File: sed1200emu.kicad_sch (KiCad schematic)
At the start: 17 parts, among them CN1 PINHD-1X6, CN2 PINHD-1X6, IC1 MEGA8-AI, Q1 CRYSTALHC49S

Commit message: Replace MEGA8 Symbol and Footprint
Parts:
- IC1: footprint sed1200emu:TQFP32-08 -> Package_QFP:TQFP-32_7x7mm_P0.8mm
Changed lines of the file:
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@@
   (symbol (lib_id "sed1200emu-eagle-import:VCC") (at 180.34 93.98 90) (unit 1)
     (in_bom yes) (on_board yes) (dnp no)
-    (property "Reference" "#P+3" (at 180.34 93.98 0)
+    (property "Reference" "#P+03" (at 180.34 93.98 0)
       (effects (font (size 1.27 1.27)) hide)
     )
@@
       (project "sed1200emu"
         (path "/123507c6-0003-4611-af8b-4b1000037212"
-          (reference "#P+3") (unit 1)
+          (reference "#P+03") (unit 1)
         )
       )
@@
   (symbol (lib_id "sed1200emu-eagle-import:GND") (at 185.42 66.04 270) (unit 1)
     (in_bom yes) (on_board yes) (dnp no)
-    (property "Reference" "#GND2" (at 185.42 66.04 0)
+    (property "Reference" "#GND02" (at 185.42 66.04 0)
       (effects (font (size 1.27 1.27)) hide)
     )
@@
       (project "sed1200emu"
         (path "/123507c6-0003-4611-af8b-4b1000037212"
-          (reference "#GND2") (unit 1)
+          (reference "#GND02") (unit 1)
         )
       )
@@
   (symbol (lib_id "sed1200emu-eagle-import:GND") (at 198.12 91.44 270) (unit 1)
     (in_bom yes) (on_board yes) (dnp no)
-    (property "Reference" "#GND3" (at 198.12 91.44 0)
+    (property "Reference" "#GND03" (at 198.12 91.44 0)
       (effects (font (size 1.27 1.27)) hide)
     )
@@
       (project "sed1200emu"
         (path "/123507c6-0003-4611-af8b-4b1000037212"
-          (reference "#GND3") (unit 1)
+          (reference "#GND03") (unit 1)
         )
       )
@@
   (symbol (lib_id "sed1200emu-eagle-import:VCC") (at 165.1 127 90) (unit 1)
     (in_bom yes) (on_board yes) (dnp no)
-    (property "Reference" "#P+4" (at 165.1 127 0)
+    (property "Reference" "#P+04" (at 165.1 127 0)
       (effects (font (size 1.27 1.27)) hide)
     )
@@
       (project "sed1200emu"
         (path "/123507c6-0003-4611-af8b-4b1000037212"
-          (reference "#P+4") (unit 1)
+          (reference "#P+04") (unit 1)
         )
       )
@@
   (symbol (lib_id "sed1200emu-eagle-import:GND") (at 68.58 78.74 270) (unit 1)
     (in_bom yes) (on_board yes) (dnp no)
-    (property "Reference" "#GND9" (at 68.58 78.74 0)
+    (property "Reference" "#GND09" (at 68.58 78.74 0)
       (effects (font (size 1.27 1.27)) hide)
     )
@@
       (project "sed1200emu"
         (path "/123507c6-0003-4611-af8b-4b1000037212"
-          (reference "#GND9") (unit 1)
+          (reference "#GND09") (unit 1)
         )
       )
@@
   (symbol (lib_id "sed1200emu-eagle-import:GND") (at 198.12 129.54 270) (unit 1)
     (in_bom yes) (on_board yes) (dnp no)
-    (property "Reference" "#GND10" (at 198.12 129.54 0)
+    (property "Reference" "#GND010" (at 198.12 129.54 0)
       (effects (font (size 1.27 1.27)) hide)
     )
@@
       (project "sed1200emu"
         (path "/123507c6-0003-4611-af8b-4b1000037212"
-          (reference "#GND10") (unit 1)
+          (reference "#GND010") (unit 1)
         )
       )
@@
       (effects (font (size 1.778 1.5113)) (justify left bottom))
     )
-    (property "Footprint" "sed1200emu:TQFP32-08" (at 124.46 86.36 0)
-      (effects (font (size 1.27 1.27)) hide)
-    )
-    (property "Datasheet" "" (at 124.46 86.36 0)
+    (property "Footprint" "Package_QFP:TQFP-32_7x7mm_P0.8mm" (at 124.46 86.36 0)
+      (effects (font (size 1.27 1.27)) hide)
+    )
+    (property "Datasheet" "http://ww1.microchip.com/downloads/en/DeviceDoc/atmel-2486-8-bit-avr-microcontroller-atmega8_l_datasheet.pdf" (at 124.46 86.36 0)
       (effects (font (size 1.27 1.27)) hide)
     )
@@
   (symbol (lib_id "sed1200emu-eagle-import:GND") (at 93.98 109.22 0) (unit 1)
     (in_bom yes) (on_board yes) (dnp no)
-    (property "Reference" "#GND4" (at 93.98 109.22 0)
+    (property "Reference" "#GND04" (at 93.98 109.22 0)
       (effects (font (size 1.27 1.27)) hide)
     )
@@
       (project "sed1200emu"
         (path "/123507c6-0003-4611-af8b-4b1000037212"
-          (reference "#GND4") (unit 1)
+          (reference "#GND04") (unit 1)
         )
       )
@@
   (symbol (lib_id "sed1200emu-eagle-import:VCC") (at 81.28 48.26 0) (unit 1)
     (in_bom yes) (on_board yes) (dnp no)
-    (property "Reference" "#P+6" (at 81.28 48.26 0)
+    (property "Reference" "#P+06" (at 81.28 48.26 0)
       (effects (font (size 1.27 1.27)) hide)
     )
@@
       (project "sed1200emu"
         (path "/123507c6-0003-4611-af8b-4b1000037212"
-          (reference "#P+6") (unit 1)
+          (reference "#P+06") (unit 1)
         )
       )
@@
   (symbol (lib_id "sed1200emu-eagle-import:VCC") (at 86.36 71.12 90) (unit 1)
     (in_bom yes) (on_board yes) (dnp no)
-    (property "Reference" "#P+2" (at 86.36 71.12 0)
+    (property "Reference" "#P+02" (at 86.36 71.12 0)
       (effects (font (size 1.27 1.27)) hide)
     )
@@
       (project "sed1200emu"
         (path "/123507c6-0003-4611-af8b-4b1000037212"
-          (reference "#P+2") (unit 1)
+          (reference "#P+02") (unit 1)
         )
       )
@@
   (symbol (lib_id "sed1200emu-eagle-import:VCC") (at 187.96 142.24 270) (unit 1)
     (in_bom yes) (on_board yes) (dnp no)
-    (property "Reference" "#P+5" (at 187.96 142.24 0)
+    (property "Reference" "#P+05" (at 187.96 142.24 0)
       (effects (font (size 1.27 1.27)) hide)
     )
@@
       (project "sed1200emu"
         (path "/123507c6-0003-4611-af8b-4b1000037212"
-          (reference "#P+5") (unit 1)
+          (reference "#P+05") (unit 1)
         )
       )
@@
   (symbol (lib_id "sed1200emu-eagle-import:GND") (at 99.06 109.22 0) (unit 1)
     (in_bom yes) (on_board yes) (dnp no)
-    (property "Reference" "#GND1" (at 99.06 109.22 0)
+    (property "Reference" "#GND01" (at 99.06 109.22 0)
       (effects (font (size 1.27 1.27)) hide)
     )
@@
       (project "sed1200emu"
         (path "/123507c6-0003-4611-af8b-4b1000037212"
-          (reference "#GND1") (unit 1)
+          (reference "#GND01") (unit 1)
         )
       )
@@
   (symbol (lib_id "sed1200emu-eagle-import:VCC") (at 182.88 45.72 90) (unit 1)
     (in_bom yes) (on_board yes) (dnp no)
-    (property "Reference" "#P+1" (at 182.88 45.72 0)
+    (property "Reference" "#P+01" (at 182.88 45.72 0)
       (effects (font (size 1.27 1.27)) hide)
     )
@@
       (project "sed1200emu"
         (path "/123507c6-0003-4611-af8b-4b1000037212"
-          (reference "#P+1") (unit 1)
+          (reference "#P+01") (unit 1)
         )
       )
@@
   (symbol (lib_id "sed1200emu-eagle-import:GND") (at 88.9 109.22 0) (unit 1)
     (in_bom yes) (on_board yes) (dnp no)
-    (property "Reference" "#GND5" (at 88.9 109.22 0)
+    (property "Reference" "#GND05" (at 88.9 109.22 0)
       (effects (font (size 1.27 1.27)) hide)
     )
@@
       (project "sed1200emu"
         (path "/123507c6-0003-4611-af8b-4b1000037212"
-          (reference "#GND5") (unit 1)
+          (reference "#GND05") (unit 1)
         )
       )
@@
   (symbol (lib_id "sed1200emu-eagle-import:GND") (at 182.88 160.02 0) (unit 1)
     (in_bom yes) (on_board yes) (dnp no)
-    (property "Reference" "#GND7" (at 182.88 160.02 0)
+    (property "Reference" "#GND07" (at 182.88 160.02 0)
       (effects (font (size 1.27 1.27)) hide)
     )
@@
       (project "sed1200emu"
         (path "/123507c6-0003-4611-af8b-4b1000037212"
-          (reference "#GND7") (unit 1)
+          (reference "#GND07") (unit 1)
         )
       )
@@
   (symbol (lib_id "sed1200emu-eagle-import:GND") (at 68.58 83.82 270) (unit 1)
     (in_bom yes) (on_board yes) (dnp no)
-    (property "Reference" "#GND8" (at 68.58 83.82 0)
+    (property "Reference" "#GND08" (at 68.58 83.82 0)
       (effects (font (size 1.27 1.27)) hide)
     )
@@
       (project "sed1200emu"
         (path "/123507c6-0003-4611-af8b-4b1000037212"
-          (reference "#GND8") (unit 1)
+          (reference "#GND08") (unit 1)
         )
       )
@@
   (symbol (lib_id "sed1200emu-eagle-import:GND") (at 198.12 101.6 270) (unit 1)
     (in_bom yes) (on_board yes) (dnp no)
-    (property "Reference" "#GND6" (at 198.12 101.6 0)
+    (property "Reference" "#GND06" (at 198.12 101.6 0)
       (effects (font (size 1.27 1.27)) hide)
     )
@@
       (project "sed1200emu"
         (path "/123507c6-0003-4611-af8b-4b1000037212"
-          (reference "#GND6") (unit 1)
-        )
-      )
+          (reference "#GND06") (unit 1)
+        )
+      )

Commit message: Replace CN1 and CN2 with KiCad Symbols
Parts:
- CN1, CN2: footprint sed1200emu:1X06 -> Connector_PinHeader_2.54mm:PinHeader_1x06_P2.54mm_Vertical
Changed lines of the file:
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@@
       (effects (font (size 1.778 1.5113)) (justify left bottom) hide)
     )
-    (property "Footprint" "sed1200emu:1X06" (at 195.58 53.34 0)
+    (property "Footprint" "Connector_PinHeader_2.54mm:PinHeader_1x06_P2.54mm_Vertical" (at 195.58 53.34 0)
       (effects (font (size 1.27 1.27)) hide)
     )
@@
       (effects (font (size 1.778 1.5113)) (justify left bottom) hide)
     )
-    (property "Footprint" "sed1200emu:1X06" (at 195.58 73.66 0)
-      (effects (font (size 1.27 1.27)) hide)
-    )
+    (property "Footprint" "Connector_PinHeader_2.54mm:PinHeader_1x06_P2.54mm_Vertical" (at 195.58 73.66 0)
+      (effects (font (size 1.27 1.27)) hide)
+    )

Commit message: Replace all 1pin out headers to KiCad Symbols
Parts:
- removed MISO0: MISO, sed1200emu:2,15_1,0, symbol sed1200emu-eagle-import:2,15/1,0
- removed MOSI0: MOSI, sed1200emu:2,15_1,0, symbol sed1200emu-eagle-import:2,15/1,0
- removed PGND1, PGND2: 2,15/1,0, sed1200emu:2,15_1,0, symbol sed1200emu-eagle-import:2,15/1,0
- removed RESET0: RESET, sed1200emu:2,15_1,0, symbol sed1200emu-eagle-import:2,15/1,0
- removed SCK0: SCK, sed1200emu:2,15_1,0, symbol sed1200emu-eagle-import:2,15/1,0
- added MISOO1, MOSIO1, PGND1, PGND2, RESETO1, SCKO1: Conn_01x01_Pin, Connector_PinHeader_2.54mm:PinHeader_1x01_P2.54mm_Vertical, symbol Connector:Conn_01x01_Pin
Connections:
- net GND: now also PGND1.1 (Pin_1), PGND2.1 (Pin_1)
- net at DIS2.14 (D7), IC1.15 (PB3(MOSI/OC2)): now also MOSIO1.1 (Pin_1)
- net at IC1.17 (PB5(SCK)): now also SCKO1.1 (Pin_1)
- net at IC1.16 (PB4(MISO)): now also MISOO1.1 (Pin_1)
- net at IC1.29 (PC6(/RESET)): now also RESETO1.1 (Pin_1)

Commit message: Update 20X2 Display Symbol & and fix pin header references
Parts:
- renumbered MISOO1 to MISO1, MOSIO1 to MOSI1, RESETO1 to RESET1, SCKO1 to SCK1
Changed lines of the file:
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@@
   (symbol (lib_id "Connector:Conn_01x01_Pin") (at 154.94 148.59 90) (unit 1)
     (in_bom yes) (on_board yes) (dnp no)
-    (property "Reference" "MISOO1" (at 154.94 152.4 0)
+    (property "Reference" "MISO1" (at 154.94 152.4 0)
       (effects (font (size 1.27 1.27)))
     )
@@
       (project "sed1200emu"
         (path "/123507c6-0003-4611-af8b-4b1000037212"
-          (reference "MISOO1") (unit 1)
+          (reference "MISO1") (unit 1)
         )
       )
@@
   (symbol (lib_id "Connector:Conn_01x01_Pin") (at 66.04 60.96 0) (unit 1)
     (in_bom yes) (on_board yes) (dnp no)
-    (property "Reference" "RESETO1" (at 62.23 60.96 0)
+    (property "Reference" "RESET1" (at 62.23 60.96 0)
       (effects (font (size 1.27 1.27)))
     )
@@
       (project "sed1200emu"
         (path "/123507c6-0003-4611-af8b-4b1000037212"
-          (reference "RESETO1") (unit 1)
+          (reference "RESET1") (unit 1)
         )
       )
@@
   (symbol (lib_id "Connector:Conn_01x01_Pin") (at 157.48 148.59 90) (unit 1)
     (in_bom yes) (on_board yes) (dnp no)
-    (property "Reference" "SCKO1" (at 157.48 152.4 0)
+    (property "Reference" "SCK1" (at 157.48 152.4 0)
       (effects (font (size 1.27 1.27)))
     )
@@
       (project "sed1200emu"
         (path "/123507c6-0003-4611-af8b-4b1000037212"
-          (reference "SCKO1") (unit 1)
+          (reference "SCK1") (unit 1)
         )
       )
@@
   (symbol (lib_id "Connector:Conn_01x01_Pin") (at 160.02 148.59 90) (unit 1)
     (in_bom yes) (on_board yes) (dnp no)
-    (property "Reference" "MOSIO1" (at 160.02 152.4 0)
+    (property "Reference" "MOSI1" (at 160.02 152.4 0)
       (effects (font (size 1.27 1.27)))
     )
@@
       (project "sed1200emu"
         (path "/123507c6-0003-4611-af8b-4b1000037212"
-          (reference "MOSIO1") (unit 1)
-        )
-      )
+          (reference "MOSI1") (unit 1)
+        )
+      )

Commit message: Update Reference Values for BOM
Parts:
- C1, C2: value 0.1 -> 0.1uF
- CN1, CN2: value PINHD-1X6 -> Conn_01x06_Pin 2.54mm
- DIS2: value TUXGR_20X2 -> SMH2002-A
- IC1: value MEGA8-AI -> ATMEGA8L-8AU
- Q1: value CRYSTALHC49S -> HC-49/S 16pF
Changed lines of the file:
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@@
       (effects (font (size 1.778 1.5113)) (justify left bottom))
     )
-    (property "Value" "CRYSTALHC49S" (at 91.44 78.74 0)
+    (property "Value" "HC-49/S 16pF" (at 91.44 78.74 0)
       (effects (font (size 1.778 1.5113)) (justify left bottom) hide)
     )
@@
       (effects (font (size 1.778 1.5113)) (justify left bottom))
     )
-    (property "Value" "MEGA8-AI" (at 106.68 57.15 0)
+    (property "Value" "ATMEGA8L-8AU" (at 106.68 57.15 0)
       (effects (font (size 1.778 1.5113)) (justify left bottom))
     )
@@
       (effects (font (size 1.778 1.5113)) (justify left bottom))
     )
-    (property "Value" "PINHD-1X6" (at 189.23 63.5 0)
+    (property "Value" "Conn_01x06_Pin 2.54mm" (at 189.23 63.5 0)
       (effects (font (size 1.778 1.5113)) (justify left bottom) hide)
     )
@@
       (effects (font (size 1.778 1.5113)) (justify left bottom))
     )
-    (property "Value" "TUXGR_20X2" (at 224.79 104.14 0)
+    (property "Value" "SMH2002-A" (at 224.79 104.14 0)
       (effects (font (size 1.778 1.5113)) (justify left bottom))
     )
@@
       (effects (font (size 1.778 1.5113)) (justify left bottom))
     )
-    (property "Value" "0.1" (at 95.504 106.299 0)
+    (property "Value" "0.1uF" (at 91.44 106.68 0)
       (effects (font (size 1.778 1.5113)) (justify left bottom))
     )
@@
       (effects (font (size 1.778 1.5113)) (justify left bottom))
     )
-    (property "Value" "PINHD-1X6" (at 189.23 83.82 0)
+    (property "Value" "Conn_01x06_Pin 2.54mm" (at 189.23 83.82 0)
       (effects (font (size 1.778 1.5113)) (justify left bottom) hide)
     )
@@
       (effects (font (size 1.778 1.5113)) (justify left bottom))
     )
-    (property "Value" "0.1" (at 90.424 106.299 0)
-      (effects (font (size 1.778 1.5113)) (justify left bottom))
+    (property "Value" "0.1uF" (at 86.36 106.68 0)
+      (effects (font (size 1.778 1.5113)) (justify bottom))
     )
     (property "Footprint" "sed1200emu:C0805" (at 88.9 101.6 0)

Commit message: Cleanup PCB, Add UART header, Consolidate SPI headers, Reset VCC Connect
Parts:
- removed MISO1, MOSI1, PGND1, PGND2, RESET1, SCK1: Conn_01x01_Pin, Connector_PinHeader_2.54mm:PinHeader_1x01_P2.54mm_Vertical, symbol Connector:Conn_01x01_Pin
- added R3: 10k, Resistor_SMD:R_0805_2012Metric, symbol Device:R
- added RESET1: Conn_01x02_Pin, Connector_PinHeader_2.54mm:PinHeader_1x02_P2.54mm_Vertical, symbol Connector:Conn_01x02_Pin
- added SPI1: Conn_01x04_Pin, Connector_PinHeader_2.54mm:PinHeader_1x04_P2.54mm_Vertical, symbol Connector:Conn_01x04_Pin
- added UART1: Conn_01x03_Pin, Connector_PinHeader_2.54mm:PinHeader_1x03_P2.54mm_Vertical, symbol Connector:Conn_01x03_Pin
- C1, C2, C3, C4: footprint sed1200emu:C0805 -> Capacitor_SMD:C_0805_2012Metric
- R1: footprint sed1200emu:M0805 -> Resistor_SMD:R_0805_2012Metric
- R2: renamed from R6; footprint sed1200emu:M0805 -> Resistor_SMD:R_0805_2012Metric
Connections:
- net GND: now also RESET1.1 (Pin_1), SPI1.1 (Pin_1), UART1.1 (Pin_1)
- net VCC: now also R3.2
- net INT1: now reaches CN1.4, IC1.1 (PD3(INT1))
- net AIN0: now reaches DIS2.4 (RS), IC1.10 (PD6(AIN0))
- net AIN1: now reaches DIS2.6 (E), IC1.11 (PD7(AIN1))
- net ICP: now reaches DIS2.11 (D4), IC1.12 (PB0(ICP))
- net OC1A: now reaches DIS2.12 (D5), IC1.13 (PB1(OC1A))
- net OC1B: now reaches DIS2.13 (D6), IC1.14 (PB2(SS/OC1B))
- net MOSI: now reaches DIS2.14 (D7), IC1.15 (PB3(MOSI/OC2))
- net MOSI: now also SPI1.2 (Pin_2)
- net MISO: now reaches IC1.16 (PB4(MISO))
- net MISO: now also SPI1.3 (Pin_3)
- net SCK: now reaches IC1.17 (PB5(SCK))
- net SCK: now also SPI1.4 (Pin_4)
- net ADC0: now reaches CN1.5, IC1.23 (PC0(ADC0))
- net ADC1: now reaches CN1.6, IC1.24 (PC1(ADC1))
- net ADC2: now reaches CN2.5, IC1.25 (PC2(ADC2))
- net ADC3: now reaches CN2.6, IC1.26 (PC3(ADC3))
- net ADC4: now reaches CN2.3, IC1.27 (PC4(ADC4/SDA))
- net at IC1.29 (PC6(/RESET)): now also R3.1, RESET1.2 (Pin_2)
- net RXD: now reaches IC1.30 (PD0(RXD))
- net RXD: now also UART1.3 (Pin_3)
- net TXD: now reaches IC1.31 (PD1(TXD))
- net TXD: now also UART1.2 (Pin_2)
- net INT0: now reaches CN1.3, IC1.32 (PD2(INT0))
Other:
- moved on the sheet: CN1, CN2, DIS2, R1, R2

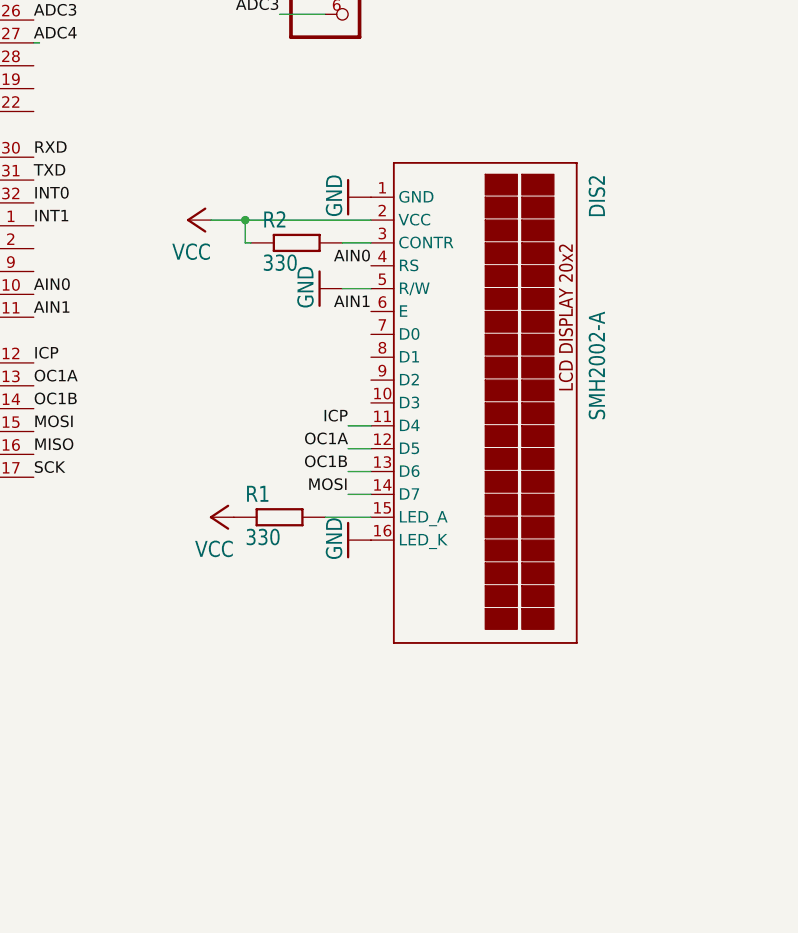
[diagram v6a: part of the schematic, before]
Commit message: Added single row HD44780 header, shifted all components up to make better use of space
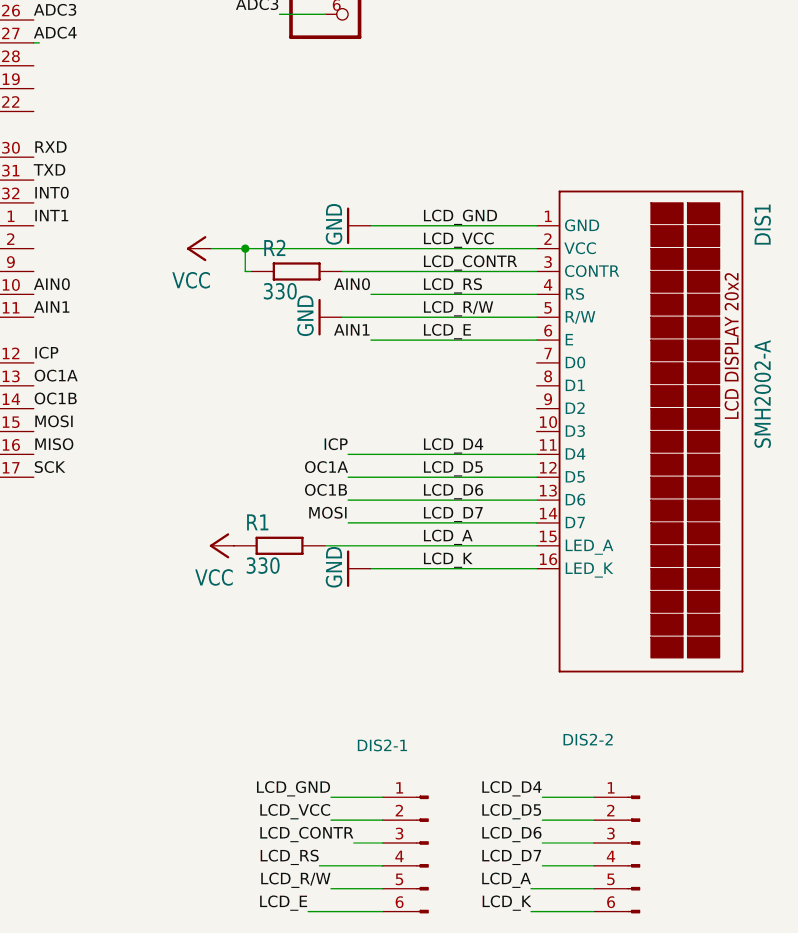
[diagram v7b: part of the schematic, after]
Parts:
- added DIS2-1, DIS2-2: Conn_01x06_Pin, Connector_PinHeader_2.54mm:PinHeader_1x06_P2.54mm_Vertical, symbol Connector:Conn_01x06_Pin
- renumbered DIS2 to DIS1
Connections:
- net AIN0: now also DIS2-1.4 (Pin_4)
- net AIN1: now also DIS2-1.6 (Pin_6)
- net GND: now also DIS2-1.1 (Pin_1), DIS2-1.5 (Pin_5), DIS2-2.6 (Pin_6)
- net ICP: now also DIS2-2.1 (Pin_1)
- net VCC: now also DIS2-1.2 (Pin_2)
- net LCD_CONTR: now reaches DIS1.3 (CONTR), R2.2
- net LCD_CONTR: now also DIS2-1.3 (Pin_3)
- net LCD_A: now reaches DIS1.15 (LED_A), R1.2
- net LCD_A: now also DIS2-2.5 (Pin_5)
- net MOSI renamed LCD_D7
- net LCD_D7: now also DIS2-2.4 (Pin_4)
- net OC1A renamed LCD_D5
- net LCD_D5: now also DIS2-2.2 (Pin_2)
- net OC1B renamed LCD_D6
- net LCD_D6: now also DIS2-2.3 (Pin_3)
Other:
- moved on the sheet: DIS1, R1, R2
